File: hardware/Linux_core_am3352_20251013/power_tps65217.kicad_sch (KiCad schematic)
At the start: 13 parts, among them SW2 SW_Push, U2 TPS65217ARSLT

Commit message: update
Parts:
- added C15, C16, C17: 10uF, symbol Device:C_Small
- added C18, C19: 2.2uF, symbol Device:C_Small
- added L1: 2.2uH, Inductor_SMD:L_1008_2520Metric_Pad1.43x2.20mm_HandSolder, symbol Device:L_Small
- added L2, L3: 2.2uH, symbol Device:L_Small
- added R12: 0Ω, symbol Device:R_Small
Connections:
- net GND: now also C15.1, C16.1, C17.1, C18.1, C19.1
- net VLDO2_3.3V: now reaches U2.1 (VLDO2)
- net VLDO2_3.3V: now also C19.2
- net PMIC_MUX_IN: now reaches U2.14 (MUX_IN)
- net PMIC_MUX_OUT: now reaches U2.16 (MUX_OUT)
- net at U2.19 (VDCDC1): now also L1.2, R12.1
- net at U2.20 (L1): now also L1.1
- net at U2.23 (L2): now also L2.1
- net VDD_MPU: now reaches U2.24 (VDCDC2)
- net VDD_MPU: now also C16.2, L2.2
- net VDD_CORE: now reaches U2.29 (VDCDC3)
- net VDD_CORE: now also C17.2, L3.2
- net at U2.31 (L3): now also L3.1
- net PMIC_ISINK2: now reaches U2.33 (ISINK2)
- net PMIC_ISINK1: now reaches U2.34 (ISINK1)
- net PMIC_ISET1: now reaches U2.35 (ISET1)
- net PMIC_ISET2: now reaches U2.36 (ISET2)
- net PMIC_L4: now reaches U2.37 (L4)
- net PMIC_FB_WLED: now reaches U2.38 (FB_WLED)
- net PMIC_LS1_OUT: now reaches U2.40 (LS1_OUT)
- net PMIC_LS2_OUT: now reaches U2.43 (LS2_OUT)
- net LDO_PGOOD renamed PMIC_LDO_PGOOD
- net SCL renamed PMIC_SCL
- net SDA renamed PMIC_SDA
- net TS renamed TEM_SENSE
- net VLDO1_1.8V renamed VLDO1
- net VLDO1: now also C18.2
- new net VDDS_DDR: C15.2, R12.2
- no-connect marks 9 -> 1
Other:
- note added: "1.8V"
- note added: "3.3V"
- note added: "IO参考电压"
- note added: "双引脚加粗输出，板外补充10uF电容"
- note removed: "双引脚加粗输出"
- note removed: "灯带待定"
- moved on the sheet: C10, C11, C12

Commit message: update
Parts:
- added C20: 10uF, symbol Device:C_Small
- added C21: 2.2uF, symbol Device:C_Small
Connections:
- net GND: now also C20.1, C21.1
- net PMIC_LS1_OUT: now also C21.2
- net PMIC_LS2_OUT: now also C20.2
- net BAT1 renamed PMIC_BAT1
- net BAT2 renamed PMIC_BAT2
- net BAT_SENSE renamed PMIC_BAT_SENSE
- net NWAKEUP renamed PMIC_NWAKEUP
- net TEM_SENSE renamed PMIC_BATTEM_SENSE
- net VLDO2_3.3V renamed PMIC_VLDO2
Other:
- note added: "1.1V"
- note added: "1.5V"
- moved on the sheet: C14, C18, C19, C6, C7

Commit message: update
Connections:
- net PMIC_POWR_EN renamed PMIC_POWER_EN
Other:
- moved on the sheet: C15, C16, C17
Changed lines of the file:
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@@
 		)
 	)
+	(text "3.3V"
+		(exclude_from_sim no)
+		(at 199.136 127.762 0)
+		(effects
+			(font
+				(size 1.27 1.27)
+			)
+		)
+	)
 	(text "1.8V"
 		(exclude_from_sim no)
@@
 		)
 	)
+	(text "1.8V"
+		(exclude_from_sim no)
+		(at 199.136 124.968 0)
+		(effects
+			(font
+				(size 1.27 1.27)
+			)
+		)
+	)
 	(junction
 		(at 203.2 125.73)
@@
 	(wire
 		(pts
-			(xy 195.58 125.73) (xy 203.2 125.73)
+			(xy 193.04 125.73) (xy 203.2 125.73)
 		)
 		(stroke
@@
 	(wire
 		(pts
-			(xy 213.36 101.6) (xy 213.36 114.3)
+			(xy 213.36 101.6) (xy 213.36 115.57)
 		)
 		(stroke
@@
 	(wire
 		(pts
+			(xy 201.93 114.3) (xy 214.63 114.3)
+		)
+		(stroke
+			(width 0)
+			(type default)
+		)
+	)
+	(wire
+		(pts
 			(xy 115.57 44.45) (xy 115.57 40.64)
 		)
@@
 	(wire
 		(pts
-			(xy 208.28 107.95) (xy 208.28 114.3)
+			(xy 208.28 107.95) (xy 208.28 115.57)
 		)
 		(stroke
@@
 	(wire
 		(pts
+			(xy 214.63 101.6) (xy 213.36 101.6)
+		)
+		(stroke
+			(width 0)
+			(type default)
+		)
+	)
+	(wire
+		(pts
 			(xy 86.36 110.49) (xy 95.25 110.49)
 		)
@@
 	(wire
 		(pts
+			(xy 208.28 107.95) (xy 214.63 107.95)
+		)
+		(stroke
+			(width 0)
+			(type default)
+		)
+	)
+	(wire
+		(pts
 			(xy 193.04 151.13) (xy 181.61 151.13)
 		)
@@
 	(wire
 		(pts
+			(xy 201.93 115.57) (xy 201.93 114.3)
+		)
+		(stroke
+			(width 0)
+			(type default)
+		)
+	)
+	(wire
+		(pts
 			(xy 110.49 69.85) (xy 113.03 69.85)
 		)
@@
 	(wire
 		(pts
-			(xy 195.58 121.92) (xy 170.18 121.92)
+			(xy 193.04 121.92) (xy 170.18 121.92)
 		)
 		(stroke
@@
 	(wire
 		(pts
-			(xy 195.58 125.73) (xy 195.58 121.92)
+			(xy 193.04 125.73) (xy 193.04 121.92)
 		)
 		(stroke
@@
 		)
 	)
+	(hierarchical_label "VDD_MPU"
+		(shape output)
+		(at 214.63 107.95 0)
+		(effects
+			(font
+				(size 1.27 1.27)
+			)
+			(justify left)
+		)
+	)
 	(hierarchical_label "PMIC_SDA"
 		(shape bidirectional)
@@
 		)
 	)
+	(hierarchical_label "VDDS_DDR"
+		(shape output)
+		(at 214.63 101.6 0)
+		(effects
+			(font
+				(size 1.27 1.27)
+			)
+			(justify left)
+		)
+	)
 	(hierarchical_label "VIN"
 		(shape input)
@@
 		)
 	)
-	(hierarchical_label "PMIC_POWR_EN"
+	(hierarchical_label "PMIC_POWER_EN"
 		(shape input)
 		(at 99.06 85.09 180)
@@
 		)
 	)
+	(hierarchical_label "VDD_CORE"
+		(shape output)
+		(at 214.63 114.3 0)
+		(effects
+			(font
+				(size 1.27 1.27)
+			)
+			(justify left)
+		)
+	)
 	(hierarchical_label "USB_DC"
 		(shape input)
@@
 	(symbol
 		(lib_id "Device:C_Small")
-		(at 208.28 116.84 180)
+		(at 208.28 118.11 180)
 		(unit 1)
 		(exclude_from_sim no)
@@
 		(dnp no)
 		(property "Reference" "C16"
-			(at 212.09 115.316 0)
+			(at 212.09 116.586 0)
 			(effects
 				(font
@@
 		)
 		(property "Value" "10uF"
-			(at 213.106 118.364 0)
+			(at 213.106 119.634 0)
 			(effects
 				(font
@@
 		)
 		(property "Footprint" ""
-			(at 208.28 116.84 0)
+			(at 208.28 118.11 0)
 			(effects
 				(font
@@
 		)
 		(property "Datasheet" "~"
-			(at 208.28 116.84 0)
+			(at 208.28 118.11 0)
 			(effects
 				(font
@@
 		)
 		(property "Description" "Unpolarized capacitor, small symbol"
-			(at 208.28 116.84 0)
+			(at 208.28 118.11 0)
 			(effects
 				(font
@@
 	(symbol
 		(lib_id "Device:C_Small")
-		(at 201.93 116.84 180)
+		(at 201.93 118.11 180)
 		(unit 1)
 		(exclude_from_sim no)
@@
 		(dnp no)
 		(property "Reference" "C17"
-			(at 205.74 115.316 0)
+			(at 205.74 116.586 0)
 			(effects
 				(font
@@
 		)
 		(property "Value" "10uF"
-			(at 206.756 118.364 0)
+			(at 206.756 119.634 0)
 			(effects
 				(font
@@
 		)
 		(property "Footprint" ""
-			(at 201.93 116.84 0)
+			(at 201.93 118.11 0)
 			(effects
 				(font
@@
 		)
 		(property "Datasheet" "~"
-			(at 201.93 116.84 0)
+			(at 201.93 118.11 0)
 			(effects
 				(font
@@
 		)
 		(property "Description" "Unpolarized capacitor, small symbol"
-			(at 201.93 116.84 0)
+			(at 201.93 118.11 0)
 			(effects
 				(font
@@
 	(symbol
 		(lib_id "Device:C_Small")
-		(at 213.36 116.84 180)
+		(at 213.36 118.11 180)
 		(unit 1)
 		(exclude_from_sim no)
@@
 		(dnp no)
 		(property "Reference" "C15"
-			(at 217.17 115.316 0)
+			(at 217.17 116.586 0)
 			(effects
 				(font
@@
 		)
 		(property "Value" "10uF"
-			(at 218.186 118.364 0)
+			(at 218.186 119.634 0)
 			(effects
 				(font
@@
 		)
 		(property "Footprint" ""
-			(at 213.36 116.84 0)
+			(at 213.36 118.11 0)
 			(effects
 				(font
@@
 		)
 		(property "Datasheet" "~"
-			(at 213.36 116.84 0)
+			(at 213.36 118.11 0)
 			(effects
 				(font
@@
 		)
 		(property "Description" "Unpolarized capacitor, small symbol"
-			(at 213.36 116.84 0)
+			(at 213.36 118.11 0)
 			(effects
 				(font
@@
 	(symbol
 		(lib_id "power:GND")
-		(at 208.28 119.38 0)
+		(at 208.28 120.65 0)
 		(unit 1)
 		(exclude_from_sim no)
@@
 		(dnp no)
 		(property "Reference" "#PWR025"
-			(at 208.28 125.73 0)
+			(at 208.28 127 0)
 			(effects
 				(font
@@
 		)
 		(property "Value" "GND"
-			(at 205.232 121.412 0)
+			(at 205.232 122.682 0)
 			(effects
 				(font
@@
 		)
 		(property "Footprint" ""
-			(at 208.28 119.38 0)
+			(at 208.28 120.65 0)
 			(effects
 				(font
@@
 		)
 		(property "Datasheet" ""
-			(at 208.28 119.38 0)
+			(at 208.28 120.65 0)
 			(effects
 				(font
@@
 		)
 		(property "Description" "Power symbol creates a global label with name \"GND\" , ground"
-			(at 208.28 119.38 0)
+			(at 208.28 120.65 0)
 			(effects
 				(font
@@
 	(symbol
 		(lib_id "power:GND")
-		(at 201.93 119.38 0)
+		(at 201.93 120.65 0)
 		(unit 1)
 		(exclude_from_sim no)
@@
 		(dnp no)
 		(property "Reference" "#PWR026"
-			(at 201.93 125.73 0)
+			(at 201.93 127 0)
 			(effects
 				(font
@@
 		)
 		(property "Value" "GND"
-			(at 198.882 121.412 0)
+			(at 198.882 122.682 0)
 			(effects
 				(font
@@
 		)
 		(property "Footprint" ""
-			(at 201.93 119.38 0)
+			(at 201.93 120.65 0)
 			(effects
 				(font
@@
 		)
 		(property "Datasheet" ""
-			(at 201.93 119.38 0)
+			(at 201.93 120.65 0)
 			(effects
 				(font
@@
 		)
 		(property "Description" "Power symbol creates a global label with name \"GND\" , ground"
-			(at 201.93 119.38 0)
+			(at 201.93 120.65 0)
 			(effects
 				(font
@@
 	(symbol
 		(lib_id "power:GND")
-		(at 213.36 119.38 0)
+		(at 213.36 120.65 0)
 		(unit 1)
 		(exclude_from_sim no)
@@
 		(dnp no)
 		(property "Reference" "#PWR022"
-			(at 213.36 125.73 0)
+			(at 213.36 127 0)
 			(effects
 				(font
@@
 		)
 		(property "Value" "GND"
-			(at 216.408 121.412 0)
+			(at 216.408 122.682 0)
 			(effects
 				(font
@@
 		)
 		(property "Footprint" ""
-			(at 213.36 119.38 0)
+			(at 213.36 120.65 0)
 			(effects
 				(font
@@
 		)
 		(property "Datasheet" ""
-			(at 213.36 119.38 0)
+			(at 213.36 120.65 0)
 			(effects
 				(font
@@
 		)
 		(property "Description" "Power symbol creates a global label with name \"GND\" , ground"
-			(at 213.36 119.38 0)
+			(at 213.36 120.65 0)
 			(effects
 				(font

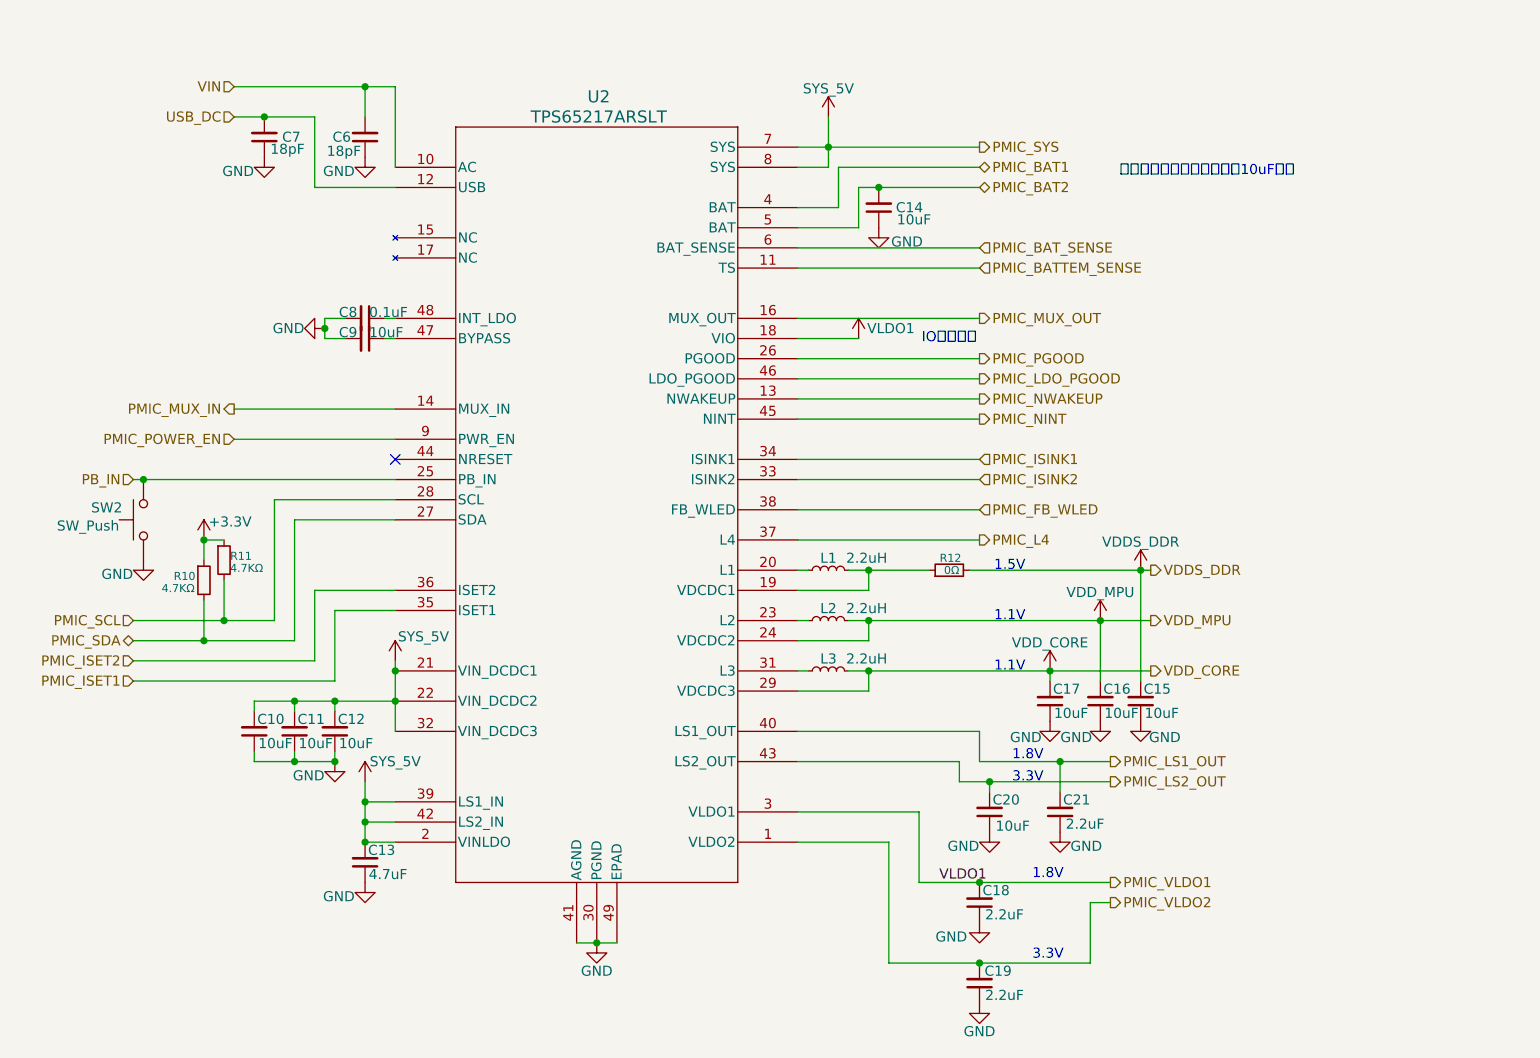
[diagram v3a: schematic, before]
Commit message: update schematic diagram
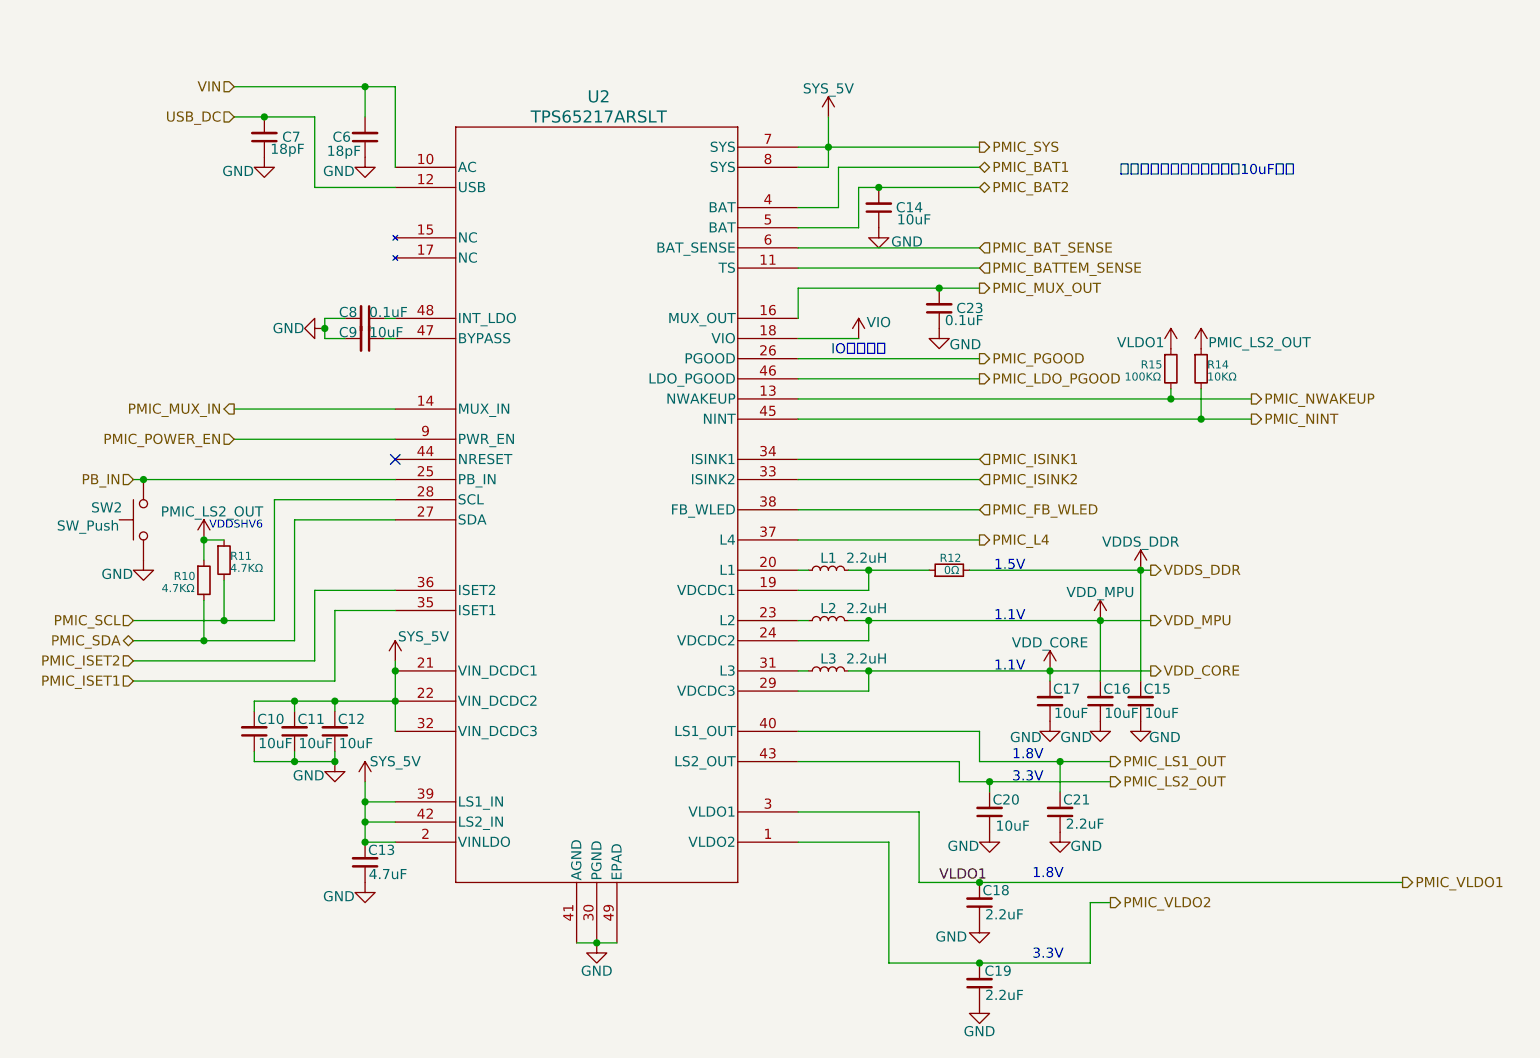
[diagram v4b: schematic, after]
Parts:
- added C23: 0.1uF, symbol Device:C_Small
- added R14: 10KΩ, symbol Device:R_Small
- added R15: 100KΩ, symbol Device:R_Small
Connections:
- net +3.3V is gone; now on net PMIC_LS2_OUT: R10.1, R11.1
- net GND: now also C23.1
- net PMIC_LS2_OUT: now also R14.1
- net PMIC_MUX_OUT: now also C23.2
- net PMIC_NINT: now also R14.2
- net PMIC_NWAKEUP: now also R15.2
- net VLDO1: now also R15.1; no longer U2.18 (VIO)
- new net VIO: U2.18 (VIO)
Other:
- note added: "VDDSHV6"
